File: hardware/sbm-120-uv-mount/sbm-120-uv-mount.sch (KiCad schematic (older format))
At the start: 15 parts, among them J1 SpringConnector, J2 SpringConnector, J3 SpringConnector, J4 SpringConnector, J5 POWER_LED

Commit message: better
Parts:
- removed H1, H4: MountingHole, MountingHole:MountingHole_3.2mm_M3, symbol Mechanical:MountingHole
- removed J1, J2, J3, J4: SpringConnector, custom_lib:TE-2286211-3, symbol Connector:Conn_01x01_Male
- added J1, J2, J3, J4: SpringConnector, custom_lib:22862113, symbol Connector:Conn_01x02_Female
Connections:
- net VDD: now also J1.1 (Pin_1), J1.2 (Pin_2), J2.1 (Pin_1), J2.2 (Pin_2)
- net VEE: now also J3.1 (Pin_1), J3.2 (Pin_2), J4.1 (Pin_1), J4.2 (Pin_2)
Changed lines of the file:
@@
 $EndDescr
-$Comp
-L Mechanical:MountingHole H1
-U 1 1 603A9329
-P 6125 1775
-F 0 "H1" H 6225 1821 50  0000 L CNN
-F 1 "MountingHole" H 6225 1730 50  0000 L CNN
-F 2 "MountingHole:MountingHole_3.2mm_M3" H 6125 1775 50  0001 C CNN
-F 3 "~" H 6125 1775 50  0001 C CNN
-	1    6125 1775
-	1    0    0    -1
-$EndComp
 $Comp
 L Mechanical:MountingHole H2
@@
 $EndComp
 $Comp
-L Mechanical:MountingHole H4
-U 1 1 603A93AD
-P 6125 2300
-F 0 "H4" H 6225 2346 50  0000 L CNN
-F 1 "MountingHole" H 6225 2255 50  0000 L CNN
-F 2 "MountingHole:MountingHole_3.2mm_M3" H 6125 2300 50  0001 C CNN
-F 3 "~" H 6125 2300 50  0001 C CNN
-	1    6125 2300
-	1    0    0    -1
-$EndComp
-$Comp
 L Mechanical:MountingHole H5
 U 1 1 603A93E7
@@
 $EndComp
 $Comp
-L Connector:Conn_01x01_Male J1
-U 1 1 603A958C
-P 2950 1800
-F 0 "J1" H 3056 1978 50  0000 C CNN
-F 1 "SpringConnector" H 3056 1887 50  0000 C CNN
-F 2 "custom_lib:TE-2286211-3" H 2950 1800 50  0001 C CNN
-F 3 "~" H 2950 1800 50  0001 C CNN
-	1    2950 1800
-	1    0    0    -1
-$EndComp
-$Comp
-L Connector:Conn_01x01_Male J2
-U 1 1 603A95DB
-P 2950 2075
-F 0 "J2" H 3056 2253 50  0000 C CNN
-F 1 "SpringConnector" H 3056 2162 50  0000 C CNN
-F 2 "custom_lib:TE-2286211-3" H 2950 2075 50  0001 C CNN
-F 3 "~" H 2950 2075 50  0001 C CNN
-	1    2950 2075
-	1    0    0    -1
-$EndComp
-$Comp
-L Connector:Conn_01x01_Male J3
-U 1 1 603A961B
-P 2950 2350
-F 0 "J3" H 3056 2528 50  0000 C CNN
-F 1 "SpringConnector" H 3056 2437 50  0000 C CNN
-F 2 "custom_lib:TE-2286211-3" H 2950 2350 50  0001 C CNN
-F 3 "~" H 2950 2350 50  0001 C CNN
-	1    2950 2350
-	1    0    0    -1
-$EndComp
-$Comp
-L Connector:Conn_01x01_Male J4
-U 1 1 603A9653
-P 2950 2600
-F 0 "J4" H 3056 2778 50  0000 C CNN
-F 1 "SpringConnector" H 3056 2687 50  0000 C CNN
-F 2 "custom_lib:TE-2286211-3" H 2950 2600 50  0001 C CNN
-F 3 "~" H 2950 2600 50  0001 C CNN
-	1    2950 2600
-	1    0    0    -1
-$EndComp
-$Comp
-L power:VDD #PWR0103
-U 1 1 603A9740
-P 3150 1800
-F 0 "#PWR0103" H 3150 1650 50  0001 C CNN
-F 1 "VDD" V 3167 1928 50  0000 L CNN
-F 2 "" H 3150 1800 50  0001 C CNN
-F 3 "" H 3150 1800 50  0001 C CNN
-	1    3150 1800
-	0    1    1    0
-$EndComp
-$Comp
-L power:VDD #PWR0104
-U 1 1 603A979A
-P 3150 2075
-F 0 "#PWR0104" H 3150 1925 50  0001 C CNN
-F 1 "VDD" V 3167 2203 50  0000 L CNN
-F 2 "" H 3150 2075 50  0001 C CNN
-F 3 "" H 3150 2075 50  0001 C CNN
-	1    3150 2075
-	0    1    1    0
-$EndComp
-$Comp
-L power:VEE #PWR0105
-U 1 1 603A9818
-P 3150 2350
-F 0 "#PWR0105" H 3150 2200 50  0001 C CNN
-F 1 "VEE" V 3167 2478 50  0000 L CNN
-F 2 "" H 3150 2350 50  0001 C CNN
-F 3 "" H 3150 2350 50  0001 C CNN
-	1    3150 2350
-	0    1    1    0
-$EndComp
-$Comp
-L power:VEE #PWR0106
-U 1 1 603A984E
-P 3150 2600
-F 0 "#PWR0106" H 3150 2450 50  0001 C CNN
-F 1 "VEE" V 3167 2728 50  0000 L CNN
-F 2 "" H 3150 2600 50  0001 C CNN
-F 3 "" H 3150 2600 50  0001 C CNN
-	1    3150 2600
-	0    1    1    0
-$EndComp
-$Comp
 L power:VEE #PWR0107
 U 1 1 603A9F72
@@
 	1    0    0    -1
 $EndComp
+$Comp
+L Connector:Conn_01x02_Female J1
+U 1 1 604134DA
+P 4050 1700
+F 0 "J1" H 4078 1676 50  0000 L CNN
+F 1 "SpringConnector" H 4078 1585 50  0000 L CNN
+F 2 "custom_lib:22862113" H 4050 1700 50  0001 C CNN
+F 3 "~" H 4050 1700 50  0001 C CNN
+	1    4050 1700
+	1    0    0    -1
+$EndComp
+$Comp
+L power:VDD #PWR0103
+U 1 1 604141D4
+P 3850 1700
+F 0 "#PWR0103" H 3850 1550 50  0001 C CNN
+F 1 "VDD" V 3867 1828 50  0000 L CNN
+F 2 "" H 3850 1700 50  0001 C CNN
+F 3 "" H 3850 1700 50  0001 C CNN
+	1    3850 1700
+	0    -1   -1   0
+$EndComp
+Wire Wire Line
+	3850 1800 3850 1700
+Connection ~ 3850 1700
+$Comp
+L Connector:Conn_01x02_Female J2
+U 1 1 60415E02
+P 4050 2000
+F 0 "J2" H 4078 1976 50  0000 L CNN
+F 1 "SpringConnector" H 4078 1885 50  0000 L CNN
+F 2 "custom_lib:22862113" H 4050 2000 50  0001 C CNN
+F 3 "~" H 4050 2000 50  0001 C CNN
+	1    4050 2000
+	1    0    0    -1
+$EndComp
+$Comp
+L power:VDD #PWR0104
+U 1 1 60415E08
+P 3850 2000
+F 0 "#PWR0104" H 3850 1850 50  0001 C CNN
+F 1 "VDD" V 3867 2128 50  0000 L CNN
+F 2 "" H 3850 2000 50  0001 C CNN
+F 3 "" H 3850 2000 50  0001 C CNN
+	1    3850 2000
+	0    -1   -1   0
+$EndComp
+Wire Wire Line
+	3850 2100 3850 2000
+Connection ~ 3850 2000
+$Comp
+L Connector:Conn_01x02_Female J3
+U 1 1 604169FD
+P 4050 2250
+F 0 "J3" H 4078 2226 50  0000 L CNN
+F 1 "SpringConnector" H 4078 2135 50  0000 L CNN
+F 2 "custom_lib:22862113" H 4050 2250 50  0001 C CNN
+F 3 "~" H 4050 2250 50  0001 C CNN
+	1    4050 2250
+	1    0    0    -1
+$EndComp
+Wire Wire Line
+	3850 2350 3850 2250
+$Comp
+L Connector:Conn_01x02_Female J4
+U 1 1 60417202
+P 4050 2500
+F 0 "J4" H 4078 2476 50  0000 L CNN
+F 1 "SpringConnector" H 4078 2385 50  0000 L CNN
+F 2 "custom_lib:22862113" H 4050 2500 50  0001 C CNN
+F 3 "~" H 4050 2500 50  0001 C CNN
+	1    4050 2500
+	1    0    0    -1
+$EndComp
+Wire Wire Line
+	3850 2600 3850 2500
+$Comp
+L power:VEE #PWR0105
+U 1 1 60417979
+P 3850 2250
+F 0 "#PWR0105" H 3850 2100 50  0001 C CNN
+F 1 "VEE" V 3867 2378 50  0000 L CNN
+F 2 "" H 3850 2250 50  0001 C CNN
+F 3 "" H 3850 2250 50  0001 C CNN
+	1    3850 2250
+	0    -1   -1   0
+$EndComp
+Connection ~ 3850 2250
+$Comp
+L power:VEE #PWR0106
+U 1 1 60418078
+P 3850 2500
+F 0 "#PWR0106" H 3850 2350 50  0001 C CNN
+F 1 "VEE" V 3867 2628 50  0000 L CNN
+F 2 "" H 3850 2500 50  0001 C CNN
+F 3 "" H 3850 2500 50  0001 C CNN
+	1    3850 2500
+	0    -1   -1   0
+$EndComp
+Connection ~ 3850 2500
 $EndSCHEMATC

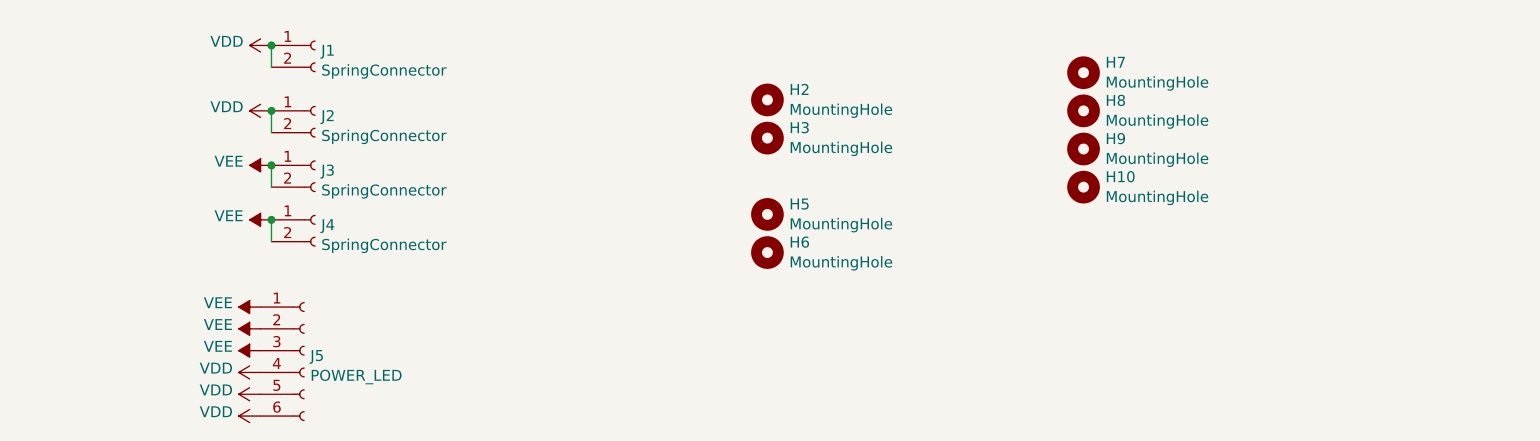
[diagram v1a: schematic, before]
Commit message: smaller and square
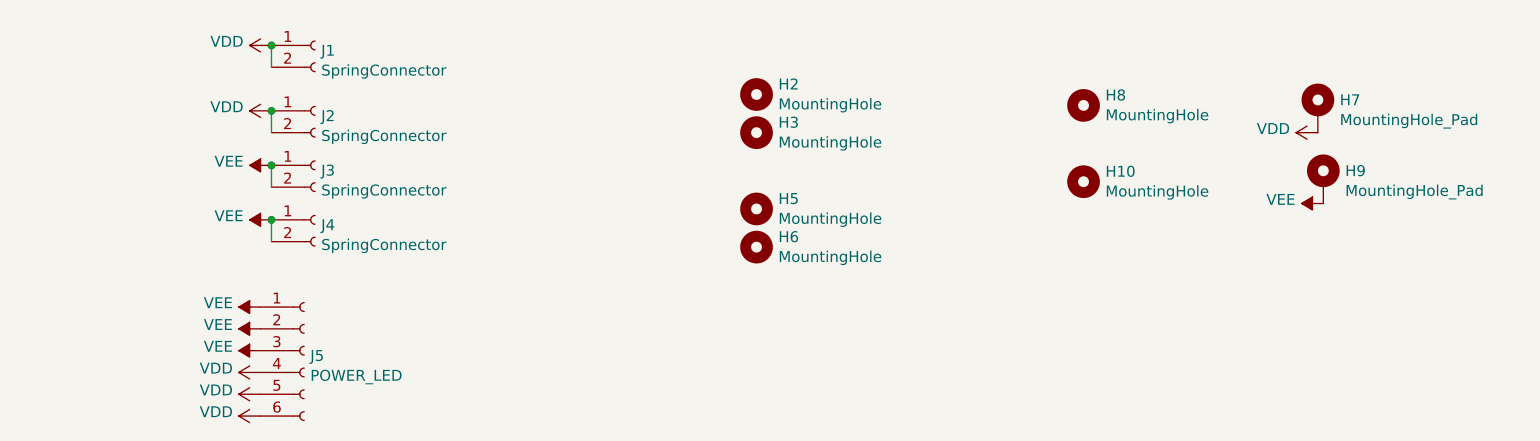
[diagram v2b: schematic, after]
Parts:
- removed H7, H9: MountingHole, MountingHole:MountingHole_2.2mm_M2, symbol Mechanical:MountingHole
- added H7, H9: MountingHole_Pad, MountingHole:MountingHole_2.2mm_M2_DIN965_Pad, symbol Mechanical:MountingHole_Pad
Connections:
- net VDD: now also H7.1
- net VEE: now also H9.1
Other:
- moved on the sheet: H10, H2, H3, H5, H6, H8
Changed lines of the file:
@@
 $EndDescr
-$Comp
-L Mechanical:MountingHole H2
-U 1 1 603A9363
-P 6125 1950
-F 0 "H2" H 6225 1996 50  0000 L CNN
-F 1 "MountingHole" H 6225 1905 50  0000 L CNN
-F 2 "MountingHole:MountingHole_3.2mm_M3" H 6125 1950 50  0001 C CNN
-F 3 "~" H 6125 1950 50  0001 C CNN
-	1    6125 1950
-	1    0    0    -1
-$EndComp
-$Comp
-L Mechanical:MountingHole H3
-U 1 1 603A9385
-P 6125 2125
-F 0 "H3" H 6225 2171 50  0000 L CNN
-F 1 "MountingHole" H 6225 2080 50  0000 L CNN
-F 2 "MountingHole:MountingHole_3.2mm_M3" H 6125 2125 50  0001 C CNN
-F 3 "~" H 6125 2125 50  0001 C CNN
-	1    6125 2125
-	1    0    0    -1
-$EndComp
-$Comp
-L Mechanical:MountingHole H5
-U 1 1 603A93E7
-P 6125 2475
-F 0 "H5" H 6225 2521 50  0000 L CNN
-F 1 "MountingHole" H 6225 2430 50  0000 L CNN
-F 2 "MountingHole:MountingHole_3.2mm_M3" H 6125 2475 50  0001 C CNN
-F 3 "~" H 6125 2475 50  0001 C CNN
-	1    6125 2475
-	1    0    0    -1
-$EndComp
-$Comp
-L Mechanical:MountingHole H6
-U 1 1 603A941B
-P 6125 2650
-F 0 "H6" H 6225 2696 50  0000 L CNN
-F 1 "MountingHole" H 6225 2605 50  0000 L CNN
-F 2 "MountingHole:MountingHole_3.2mm_M3" H 6125 2650 50  0001 C CNN
-F 3 "~" H 6125 2650 50  0001 C CNN
-	1    6125 2650
-	1    0    0    -1
-$EndComp
 $Comp
 L power:VEE #PWR0107
@@
 $EndComp
 $Comp
-L Mechanical:MountingHole H7
-U 1 1 6040D0AD
-P 7575 1825
-F 0 "H7" H 7675 1871 50  0000 L CNN
-F 1 "MountingHole" H 7675 1780 50  0000 L CNN
-F 2 "MountingHole:MountingHole_2.2mm_M2" H 7575 1825 50  0001 C CNN
-F 3 "~" H 7575 1825 50  0001 C CNN
-	1    7575 1825
-	1    0    0    -1
-$EndComp
-$Comp
 L Mechanical:MountingHole H8
 U 1 1 6040D0B3
-P 7575 2000
-F 0 "H8" H 7675 2046 50  0000 L CNN
-F 1 "MountingHole" H 7675 1955 50  0000 L CNN
-F 2 "MountingHole:MountingHole_2.2mm_M2" H 7575 2000 50  0001 C CNN
-F 3 "~" H 7575 2000 50  0001 C CNN
-	1    7575 2000
-	1    0    0    -1
-$EndComp
-$Comp
-L Mechanical:MountingHole H9
-U 1 1 6040D0B9
-P 7575 2175
-F 0 "H9" H 7675 2221 50  0000 L CNN
-F 1 "MountingHole" H 7675 2130 50  0000 L CNN
-F 2 "MountingHole:MountingHole_2.2mm_M2" H 7575 2175 50  0001 C CNN
-F 3 "~" H 7575 2175 50  0001 C CNN
-	1    7575 2175
+P 7575 1975
+F 0 "H8" H 7675 2021 50  0000 L CNN
+F 1 "MountingHole" H 7675 1930 50  0000 L CNN
+F 2 "MountingHole:MountingHole_2.2mm_M2" H 7575 1975 50  0001 C CNN
+F 3 "~" H 7575 1975 50  0001 C CNN
+	1    7575 1975
 	1    0    0    -1
 $EndComp
@@
 L Mechanical:MountingHole H10
 U 1 1 6040D0BF
-P 7575 2350
-F 0 "H10" H 7675 2396 50  0000 L CNN
-F 1 "MountingHole" H 7675 2305 50  0000 L CNN
-F 2 "MountingHole:MountingHole_2.2mm_M2" H 7575 2350 50  0001 C CNN
-F 3 "~" H 7575 2350 50  0001 C CNN
-	1    7575 2350
+P 7575 2325
+F 0 "H10" H 7675 2371 50  0000 L CNN
+F 1 "MountingHole" H 7675 2280 50  0000 L CNN
+F 2 "MountingHole:MountingHole_2.2mm_M2" H 7575 2325 50  0001 C CNN
+F 3 "~" H 7575 2325 50  0001 C CNN
+	1    7575 2325
 	1    0    0    -1
 $EndComp
@@
 $EndComp
 Connection ~ 3850 2500
+$Comp
+L Mechanical:MountingHole H6
+U 1 1 603A941B
+P 6075 2625
+F 0 "H6" H 6175 2671 50  0000 L CNN
+F 1 "MountingHole" H 6175 2580 50  0000 L CNN
+F 2 "MountingHole:MountingHole_3.2mm_M3" H 6075 2625 50  0001 C CNN
+F 3 "~" H 6075 2625 50  0001 C CNN
+	1    6075 2625
+	1    0    0    -1
+$EndComp
+$Comp
+L Mechanical:MountingHole H5
+U 1 1 603A93E7
+P 6075 2450
+F 0 "H5" H 6175 2496 50  0000 L CNN
+F 1 "MountingHole" H 6175 2405 50  0000 L CNN
+F 2 "MountingHole:MountingHole_3.2mm_M3" H 6075 2450 50  0001 C CNN
+F 3 "~" H 6075 2450 50  0001 C CNN
+	1    6075 2450
+	1    0    0    -1
+$EndComp
+$Comp
+L Mechanical:MountingHole H3
+U 1 1 603A9385
+P 6075 2100
+F 0 "H3" H 6175 2146 50  0000 L CNN
+F 1 "MountingHole" H 6175 2055 50  0000 L CNN
+F 2 "MountingHole:MountingHole_3.2mm_M3" H 6075 2100 50  0001 C CNN
+F 3 "~" H 6075 2100 50  0001 C CNN
+	1    6075 2100
+	1    0    0    -1
+$EndComp
+$Comp
+L Mechanical:MountingHole H2
+U 1 1 603A9363
+P 6075 1925
+F 0 "H2" H 6175 1971 50  0000 L CNN
+F 1 "MountingHole" H 6175 1880 50  0000 L CNN
+F 2 "MountingHole:MountingHole_3.2mm_M3" H 6075 1925 50  0001 C CNN
+F 3 "~" H 6075 1925 50  0001 C CNN
+	1    6075 1925
+	1    0    0    -1
+$EndComp
+$Comp
+L Mechanical:MountingHole_Pad H7
+U 1 1 60503DCB
+P 8650 2000
+F 0 "H7" H 8750 2049 50  0000 L CNN
+F 1 "MountingHole_Pad" H 8750 1958 50  0000 L CNN
+F 2 "MountingHole:MountingHole_2.2mm_M2_DIN965_Pad" H 8650 2000 50  0001 C CNN
+F 3 "~" H 8650 2000 50  0001 C CNN
+	1    8650 2000
+	1    0    0    -1
+$EndComp
+$Comp
+L Mechanical:MountingHole_Pad H9
+U 1 1 60505195
+P 8675 2325
+F 0 "H9" H 8775 2374 50  0000 L CNN
+F 1 "MountingHole_Pad" H 8775 2283 50  0000 L CNN
+F 2 "MountingHole:MountingHole_2.2mm_M2_DIN965_Pad" H 8675 2325 50  0001 C CNN
+F 3 "~" H 8675 2325 50  0001 C CNN
+	1    8675 2325
+	1    0    0    -1
+$EndComp
+$Comp
+L power:VDD #PWR0111
+U 1 1 60508E9D
+P 8650 2100
+F 0 "#PWR0111" H 8650 1950 50  0001 C CNN
+F 1 "VDD" V 8667 2228 50  0000 L CNN
+F 2 "" H 8650 2100 50  0001 C CNN
+F 3 "" H 8650 2100 50  0001 C CNN
+	1    8650 2100
+	0    -1   -1   0
+$EndComp
+$Comp
+L power:VEE #PWR0112
+U 1 1 6050961B
+P 8675 2425
+F 0 "#PWR0112" H 8675 2275 50  0001 C CNN
+F 1 "VEE" V 8692 2553 50  0000 L CNN
+F 2 "" H 8675 2425 50  0001 C CNN
+F 3 "" H 8675 2425 50  0001 C CNN
+	1    8675 2425
+	0    -1   -1   0
+$EndComp
 $EndSCHEMATC
